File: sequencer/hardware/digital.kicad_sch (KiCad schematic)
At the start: 36 parts

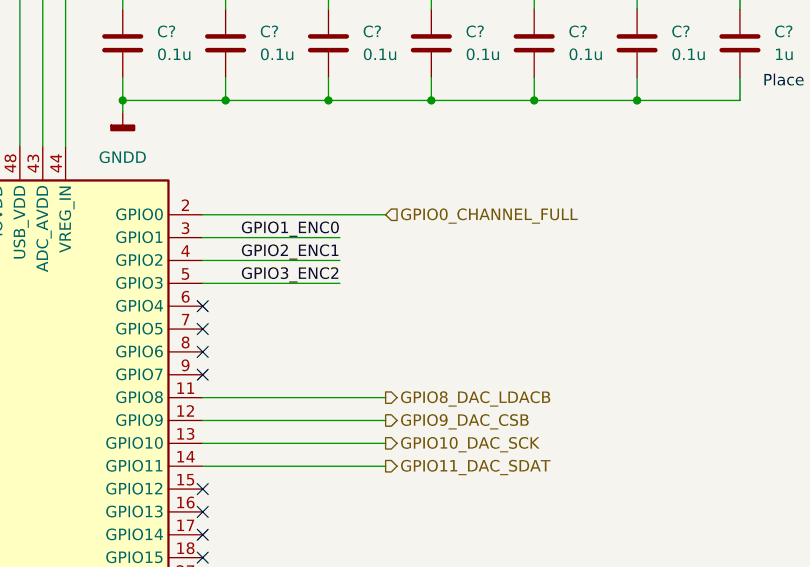
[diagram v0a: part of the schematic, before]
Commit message: Finish Sequencer Schematic
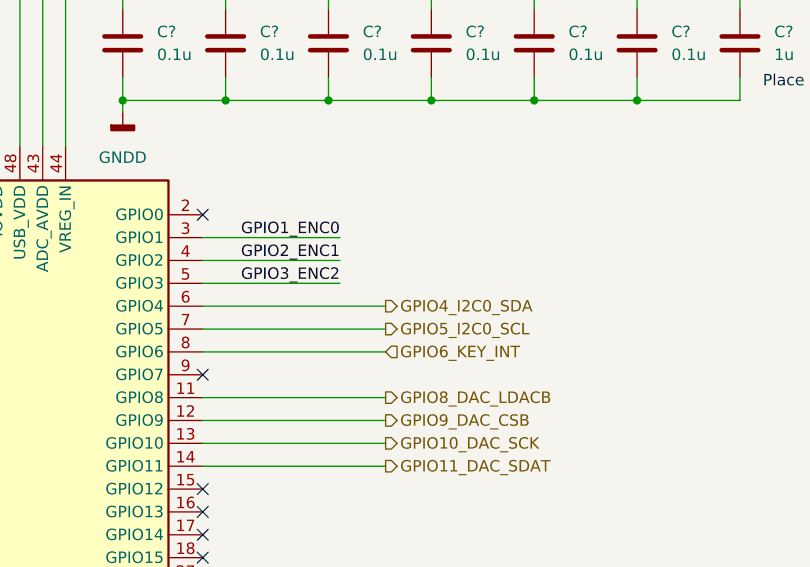
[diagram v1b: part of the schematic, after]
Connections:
- net GPIO4_I2C0_SDA: now reaches U?.6 (GPIO4)
- net GPIO5_I2C0_SCL: now reaches U?.7 (GPIO5)
- net GPIO6_KEY_INT: now reaches U?.8 (GPIO6)
- net GPIO0_CHANNEL_FULL: no longer names the net of U?.2 (GPIO0)
- no-connect marks 11 -> 9
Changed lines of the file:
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@@
   (no_connect (at 290.83 106.68))
   (no_connect (at 290.83 121.92))
-  (no_connect (at 290.83 78.74))
-  (no_connect (at 290.83 83.82))
+  (no_connect (at 290.83 68.58))
   (no_connect (at 290.83 104.14))
   (no_connect (at 290.83 124.46))
-  (no_connect (at 290.83 81.28))
   (no_connect (at 290.83 132.08))
   (wire (pts (xy 339.09 53.34) (xy 339.09 55.88))
@@
     (stroke (width 0) (type default) (color 0 0 0 0))
   )
+  (wire (pts (xy 290.83 78.74) (xy 311.15 78.74))
+    (stroke (width 0) (type default) (color 0 0 0 0))
+  )
   (wire (pts (xy 339.09 55.88) (xy 327.66 55.88))
     (stroke (width 0) (type default) (color 0 0 0 0))
@@
     (stroke (width 0) (type default) (color 0 0 0 0))
   )
-  (wire (pts (xy 290.83 68.58) (xy 311.15 68.58))
-    (stroke (width 0) (type default) (color 0 0 0 0))
-  )
   (wire (pts (xy 339.09 41.91) (xy 339.09 45.72))
     (stroke (width 0) (type default) (color 0 0 0 0))
@@
     (stroke (width 0) (type default) (color 0 0 0 0))
   )
+  (wire (pts (xy 290.83 83.82) (xy 311.15 83.82))
+    (stroke (width 0) (type default) (color 0 0 0 0))
+  )
   (wire (pts (xy 240.03 57.15) (xy 240.03 59.69))
     (stroke (width 0) (type default) (color 0 0 0 0))
@@
   )
   (wire (pts (xy 290.83 142.24) (xy 306.07 142.24))
+    (stroke (width 0) (type default) (color 0 0 0 0))
+  )
+  (wire (pts (xy 290.83 81.28) (xy 311.15 81.28))
     (stroke (width 0) (type default) (color 0 0 0 0))
   )
@@
     (effects (font (size 1.27 1.27)) (justify left))
   )
-  (hierarchical_label "GPIO0_CHANNEL_FULL" (shape input) (at 311.15 68.58 0)
-    (effects (font (size 1.27 1.27)) (justify left))
-  )
   (hierarchical_label "GPIO18_SCK" (shape input) (at 311.15 114.3 0)
     (effects (font (size 1.27 1.27)) (justify left))
@@
     (effects (font (size 1.27 1.27)) (justify right))
   )
+  (hierarchical_label "GPIO4_I2C0_SDA" (shape output) (at 311.15 78.74 0)
+    (effects (font (size 1.27 1.27)) (justify left))
+  )
   (hierarchical_label "USB_D+" (shape bidirectional) (at 207.01 73.66 180)
     (effects (font (size 1.27 1.27)) (justify right))
   )
+  (hierarchical_label "GPIO6_KEY_INT" (shape input) (at 311.15 83.82 0)
+    (effects (font (size 1.27 1.27)) (justify left))
+  )
   (hierarchical_label "GPIO8_DAC_LDACB" (shape output) (at 311.15 88.9 0)
     (effects (font (size 1.27 1.27)) (justify left))
   )
+  (hierarchical_label "GPIO5_I2C0_SCL" (shape output) (at 311.15 81.28 0)
+    (effects (font (size 1.27 1.27)) (justify left))
+  )

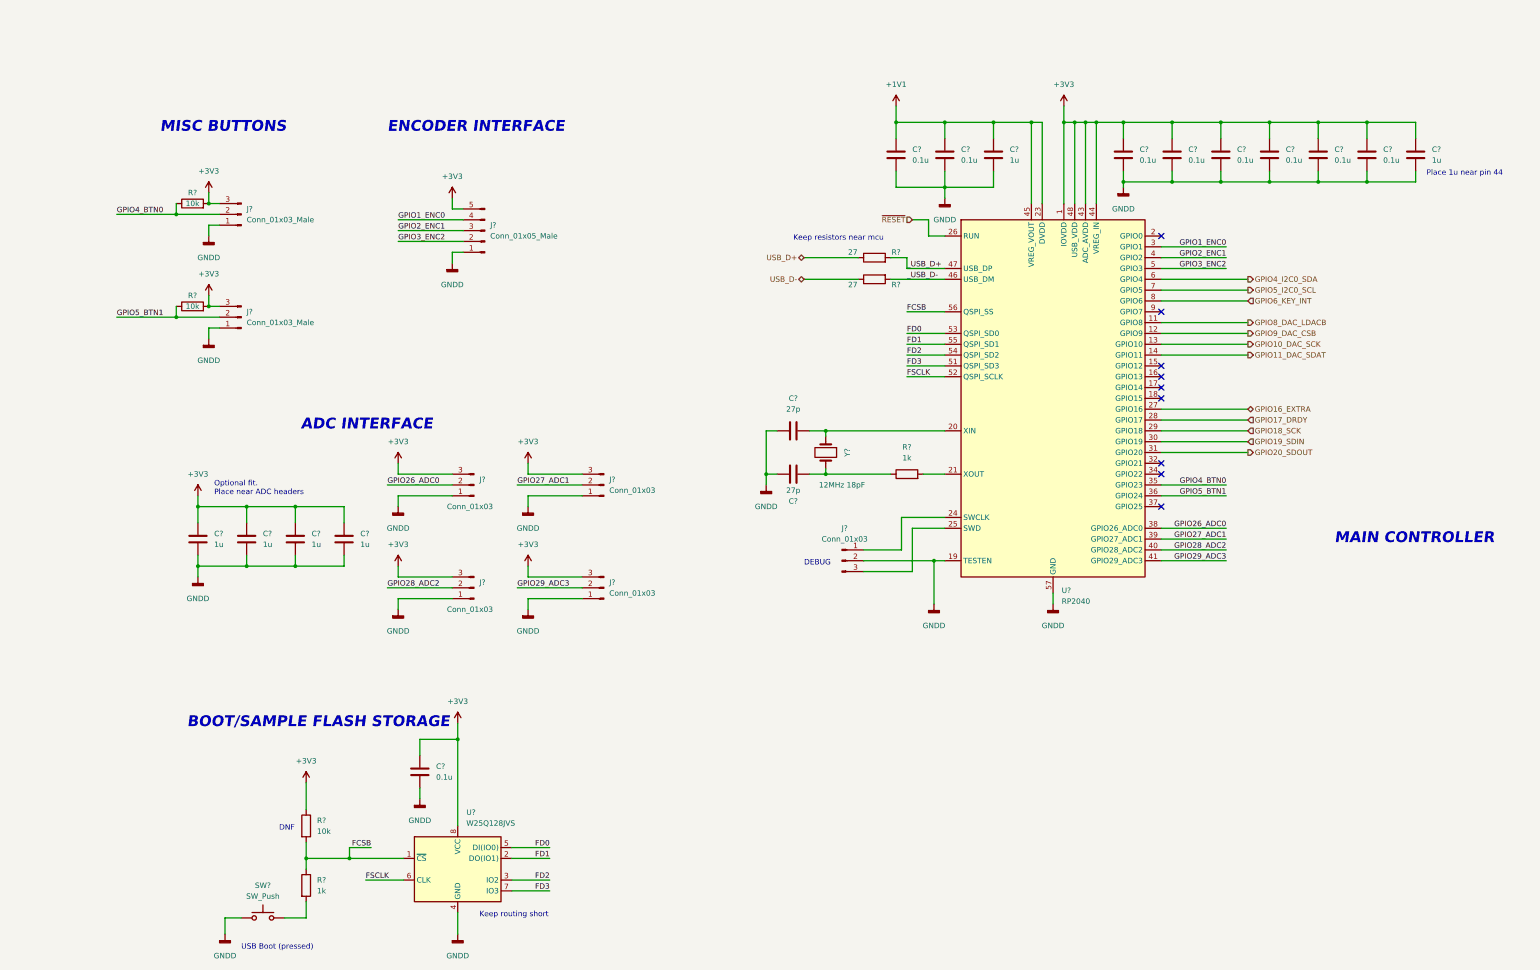
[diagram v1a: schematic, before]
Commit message: Update sequencer schematic
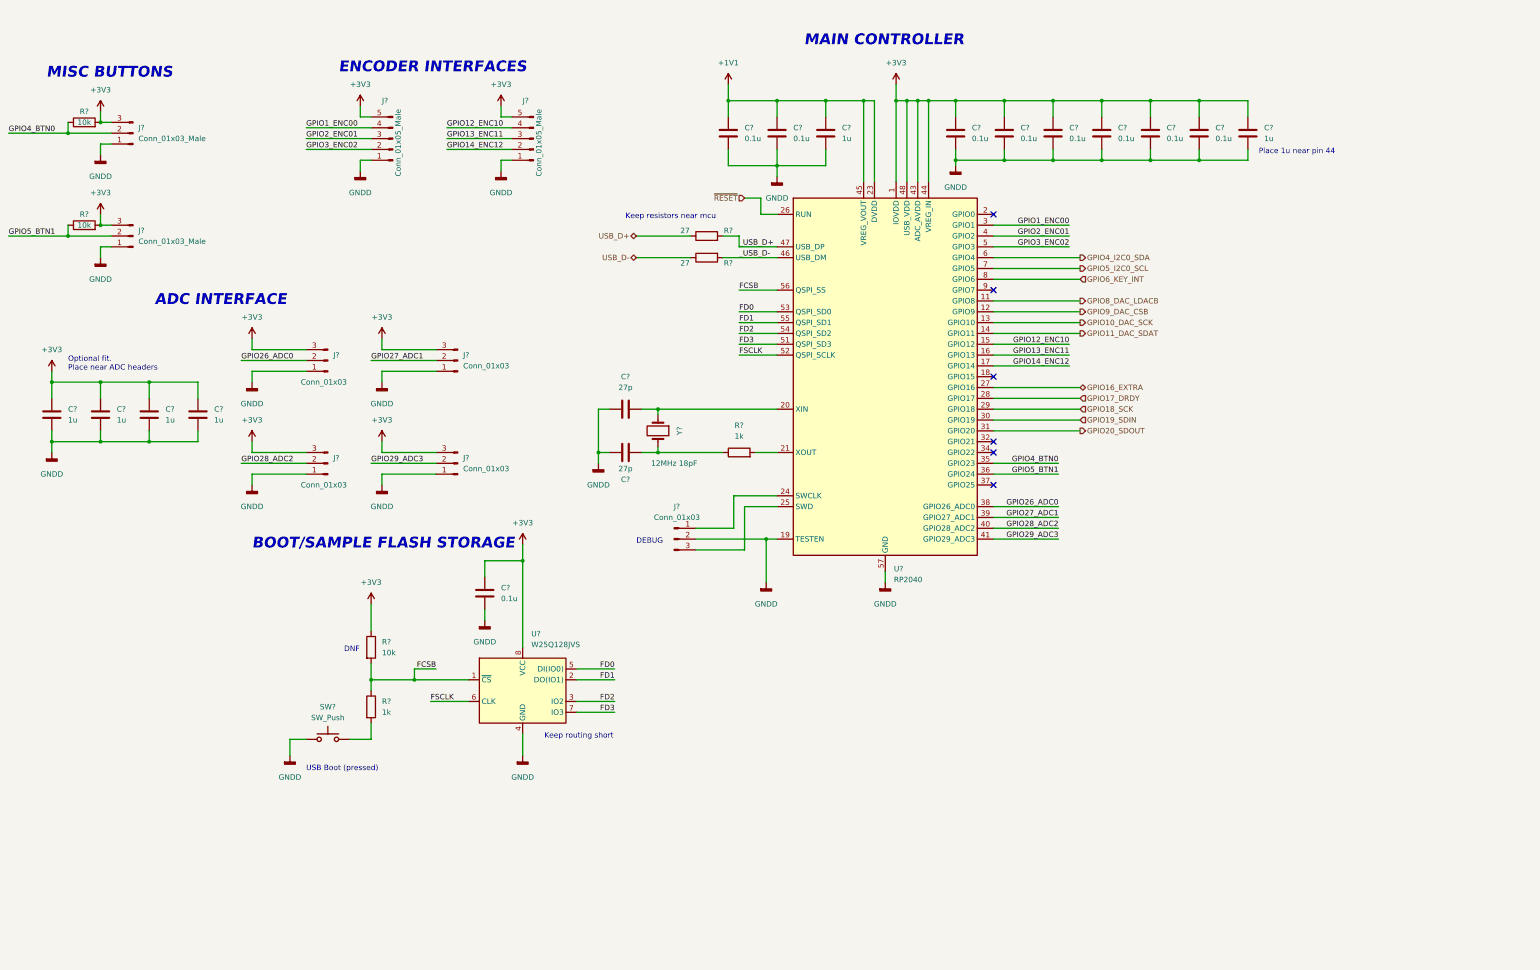
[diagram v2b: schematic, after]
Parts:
- added J?: Conn_01x05_Male, Connector_PinHeader_2.54mm:PinHeader_1x05_P2.54mm_Vertical, symbol Connector:Conn_01x05_Male
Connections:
- net +3V3: now also J?.5 (Pin_5)
- net GNDD: now also J?.1 (Pin_1)
- net GPIO12_ENC10: now reaches U?.15 (GPIO12)
- net GPIO12_ENC10: now also J?.4 (Pin_4)
- net GPIO13_ENC11: now reaches U?.16 (GPIO13)
- net GPIO13_ENC11: now also J?.3 (Pin_3)
- net GPIO14_ENC12: now reaches U?.17 (GPIO14)
- net GPIO14_ENC12: now also J?.2 (Pin_2)
- net GPIO1_ENC0 renamed GPIO1_ENC00
- net GPIO2_ENC1 renamed GPIO2_ENC01
- net GPIO3_ENC2 renamed GPIO3_ENC02
- no-connect marks 9 -> 6
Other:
- note added: "ENCODER INTERFACES"
- note removed: "ENCODER INTERFACE"
- moved on the sheet: C?, J?, R?, SW?, U?, Y?

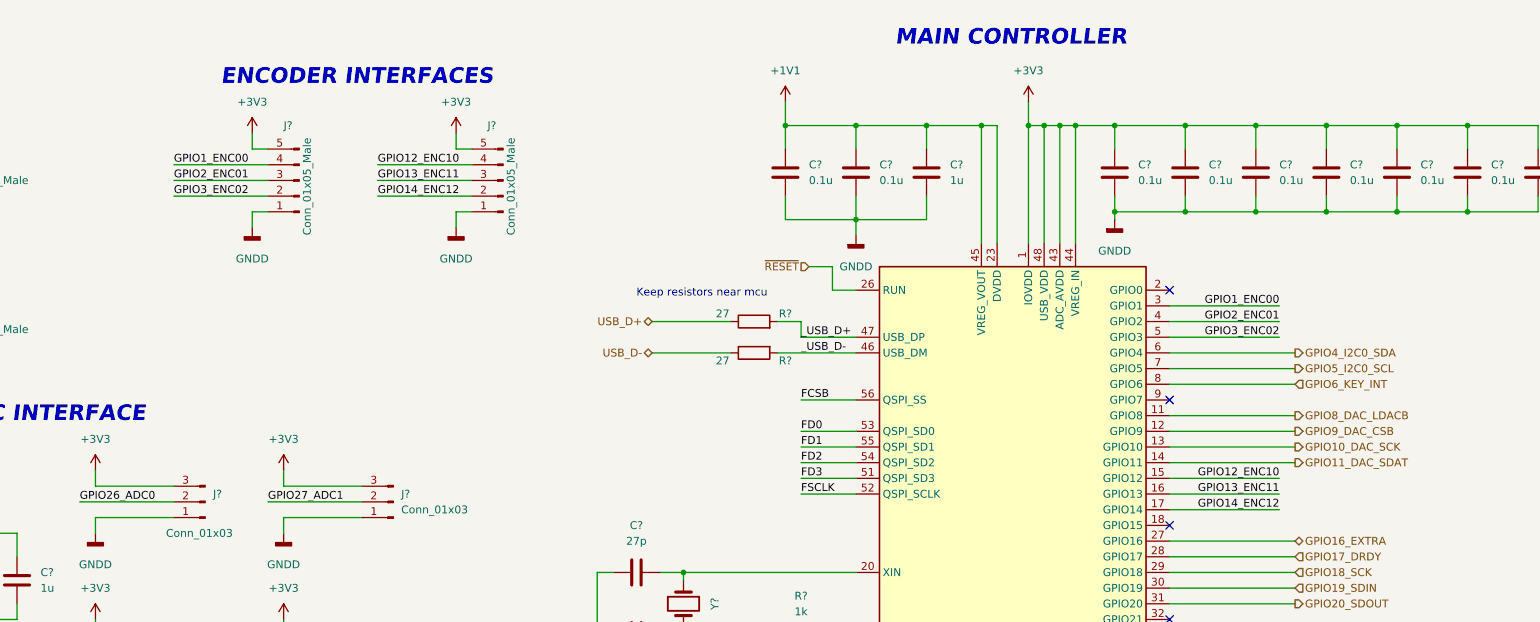
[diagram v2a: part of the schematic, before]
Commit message: Implement changes to sequencer recommended by John
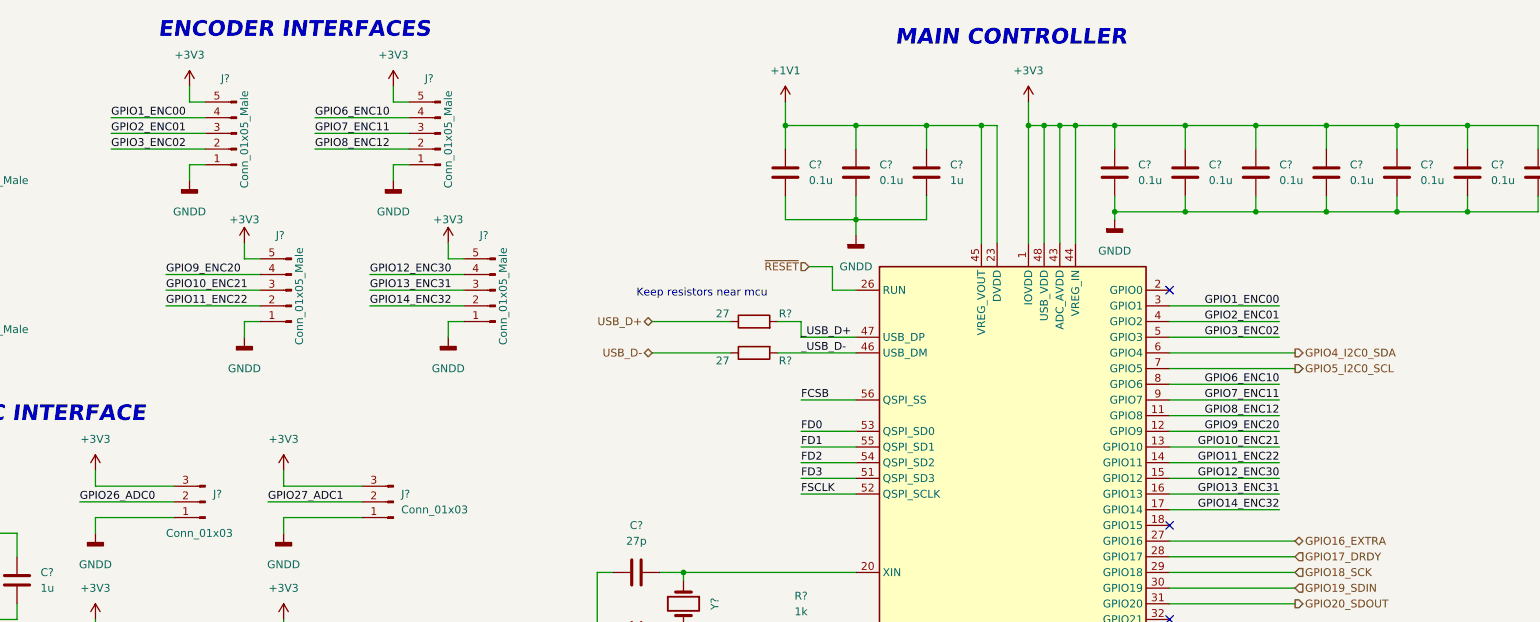
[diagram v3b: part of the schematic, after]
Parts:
- added J? (x2): Conn_01x05_Male, Connector_PinHeader_2.54mm:PinHeader_1x05_P2.54mm_Vertical, symbol Connector:Conn_01x05_Male
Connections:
- net +3V3: now also J?.5 (Pin_5), J?.5 (Pin_5)
- net GNDD: now also J?.1 (Pin_1), J?.1 (Pin_1)
- net GPIO7_ENC11: now reaches U?.9 (GPIO7)
- net GPIO7_ENC11: now also J?.3 (Pin_3)
- net GPIO10_DAC_SCK renamed GPIO10_ENC21
- net GPIO10_ENC21: now also J?.3 (Pin_3)
- net GPIO11_DAC_SDAT renamed GPIO11_ENC22
- net GPIO11_ENC22: now also J?.2 (Pin_2)
- net GPIO12_ENC10 renamed GPIO12_ENC30
- net GPIO12_ENC30: now also J?.4 (Pin_4); no longer J?.4 (Pin_4)
- net GPIO13_ENC11 renamed GPIO13_ENC31
- net GPIO13_ENC31: now also J?.3 (Pin_3); no longer J?.3 (Pin_3)
- net GPIO14_ENC12 renamed GPIO14_ENC32
- net GPIO14_ENC32: now also J?.2 (Pin_2); no longer J?.2 (Pin_2)
- net GPIO6_KEY_INT renamed GPIO6_ENC10
- net GPIO6_ENC10: now also J?.4 (Pin_4)
- net GPIO8_DAC_LDACB renamed GPIO8_ENC12
- net GPIO8_ENC12: now also J?.2 (Pin_2)
- net GPIO9_DAC_CSB renamed GPIO9_ENC20
- net GPIO9_ENC20: now also J?.4 (Pin_4)
- no-connect marks 6 -> 5
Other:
- moved on the sheet: J?

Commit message: Fix scan chain pin labeling on input connector
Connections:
- net GPIO16_NEXTPRSNT: now reaches U?.18 (GPIO15)
- no-connect marks 5 -> 4
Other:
- company: (none) -> D.R.U.M.
- title: (none) -> DRUM System Sequencer
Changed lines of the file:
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@@
 (kicad_sch (version 20211123) (generator eeschema)
   (paper "USLegal")
+  (title_block
+    (title "DRUM System Sequencer")
+    (date "2022-10-12")
+    (rev "1.0")
+    (company "D.R.U.M.")
+  )
   (junction (at 34.29 68.58) (diameter 0) (color 0 0 0 0)
   )
@@
   (junction (at 189.23 36.83) (diameter 0) (color 0 0 0 0)
   )
-  (no_connect (at 251.46 101.6))
   (no_connect (at 251.46 116.84))
   (no_connect (at 251.46 63.5))
@@
     (stroke (width 0) (type default) (color 0 0 0 0))
   )
+  (wire (pts (xy 251.46 101.6) (xy 271.78 101.6))
+    (stroke (width 0) (type default) (color 0 0 0 0))
+  )
   (wire (pts (xy 92.71 33.02) (xy 95.25 33.02))
     (stroke (width 0) (type default) (color 0 0 0 0))
@@
     (effects (font (size 1.27 1.27)) (justify right))
   )
+  (hierarchical_label "GPIO16_NEXTPRSNT" (shape input) (at 271.78 101.6 0)
+    (effects (font (size 1.27 1.27)) (justify left))
+  )
   (hierarchical_label "GPIO5_I2C0_SCL" (shape output) (at 271.78 76.2 0)

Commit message: Add filter sections to encoders
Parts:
- removed J? (x4): Conn_01x05_Male, Connector_PinHeader_2.54mm:PinHeader_1x05_P2.54mm_Vertical, symbol Connector:Conn_01x05_Male
- added C37, C38, C39, C40, C41, C42, C43, C44: 0.01u, symbol Device:C
- added J11, J12, J15, J16: JST_4-pin, symbol Connector:Conn_01x04_Male
- added R22, R23, R24, R25, R26, R27, R28, R29, R30, R31, R32, R33, R34, R35, R36, R37: 10k, symbol Device:R
- gave numbers to parts that had none: 35
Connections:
- net +3V3: now also R24.2, R25.2, R28.2, R29.2, R32.2, R33.2, R36.2, R37.2
- net GNDD: now also C37.2, C38.2, C39.2, C40.2, C41.2, C42.2, C43.2, C44.2, J11.2 (Pin_2), J12.2 (Pin_2), J15.2 (Pin_2), J16.2 (Pin_2)
- net GPIO12_ENC30: now also C44.1, R34.1
- net GPIO13_ENC31: now also C43.1, R35.1
- net GPIO1_ENC00: now also C38.1, R22.1
- net GPIO2_ENC01: now also C37.1, R23.1
- net GPIO6_ENC10: now also C42.1, R30.1
- net GPIO7_ENC11: now also C41.1, R31.1
- new net: J12.3 (Pin_3), R27.2, R28.1
- new net: J11.1 (Pin_1), R22.2, R25.1
- new net: J11.3 (Pin_3), R23.2, R24.1
- new net: J12.1 (Pin_1), R26.2, R29.1
- new net: C40.1, R26.1
- new net: J15.1 (Pin_1), R30.2, R33.1
- new net: J15.3 (Pin_3), R31.2, R32.1
- new net: C39.1, R27.1
- new net: J16.1 (Pin_1), R34.2, R37.1
- new net: J16.3 (Pin_3), R35.2, R36.1
- no-connect marks 4 -> 8
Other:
- note added: "A"
- note added: "B"
- note added: "C"
- note added: "NC"
- moved on the sheet: J7, J8, R15, R16

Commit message: Disconnect GNDD from GNDA to prevent routing confusion
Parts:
- C37, C38, C39, C40, C41, C42, C43, C44: footprint (none) -> Capacitor_SMD:C_0805_2012Metric_Pad1.18x1.45mm_HandSolder
- J11, J12, J15, J16: value JST_4-pin -> JST_4-pin_male; footprint (none) -> Connector_JST:JST_PH_B4B-PH-K_1x04_P2.00mm_Vertical
- R22, R23, R24, R25, R26, R27, R28, R29, R30, R31, R32, R33, R34, R35, R36, R37: footprint (none) -> Resistor_SMD:R_0603_1608Metric_Pad0.98x0.95mm_HandSolder
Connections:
- net GPIO10_ENC21: now also C39.1, R27.1
- net GPIO9_ENC20: now also C40.1, R26.1
- net GPIO11_ENC22: no longer names the net of U7.14 (GPIO11)
- net GPIO14_ENC32: no longer names the net of U7.17 (GPIO14)
- net GPIO3_ENC02: no longer names the net of U7.5 (GPIO3)
- net GPIO8_ENC12: no longer names the net of U7.11 (GPIO8)
- no-connect marks 8 -> 12

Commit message: Do a lot of random stuff
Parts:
- renumbered C37 to C21, C21 to C22, C38 to C23, C22 to C24, C39 to C25, C23 to C26, C40 to C27, C41 to C28, C42 to C29, C43 to C30, C44 to C31, C24 to C32, C25 to C33, C26 to C34, C27 to C35, C28 to C36, C29 to C37, C30 to C38, C31 to C39, C32 to C40, C33 to C41, C34 to C42, C35 to C43, C36 to C44, J12 to J10, J9 to J11, J10 to J12, J11 to J9, R22 to R17, R23 to R18, R24 to R19, R25 to R20, R26 to R21, R27 to R22, R28 to R23, R29 to R24, R17 to R25, R18 to R26, R30 to R27, R31 to R28, R32 to R29, R33 to R30, R34 to R31, R35 to R32, R36 to R33, R37 to R34, R19 to R35, R20 to R36, R21 to R37, U6 to U7, U7 to U8

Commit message: more library weirdness
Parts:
- U8: footprint Package_DFN_QFN:QFN-56-1EP_7x7mm_P0.4mm_EP3.2x3.2mm -> custom:QFN-56-1EP_7x7mm_P0.4mm_EP3.2x3.2mm
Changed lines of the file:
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@@
   (symbol (lib_id "MCU_RaspberryPi:RP2040") (at 226.06 101.6 0) (unit 1)
     (in_bom yes) (on_board yes) (fields_autoplaced)
-    (property "Reference" "U8" (id 0) (at 228.0794 146.685 0)
+    (property "Reference" "U8" (id 0) (at 228.0794 146.05 0)
       (effects (font (size 1.27 1.27)) (justify left))
     )
-    (property "Value" "RP2040" (id 1) (at 228.0794 149.225 0)
+    (property "Value" "RP2040" (id 1) (at 228.0794 148.59 0)
       (effects (font (size 1.27 1.27)) (justify left))
     )
-    (property "Footprint" "Package_DFN_QFN:QFN-56-1EP_7x7mm_P0.4mm_EP3.2x3.2mm" (id 2) (at 226.06 101.6 0)
+    (property "Footprint" "custom:QFN-56-1EP_7x7mm_P0.4mm_EP3.2x3.2mm" (id 2) (at 226.06 101.6 0)
       (effects (font (size 1.27 1.27)) hide)
     )
